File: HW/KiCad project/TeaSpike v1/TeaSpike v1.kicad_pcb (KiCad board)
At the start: 2 copper layers, 90 x 85 mm, 23 parts, among them U1 TP4056, U2 PowerBoost

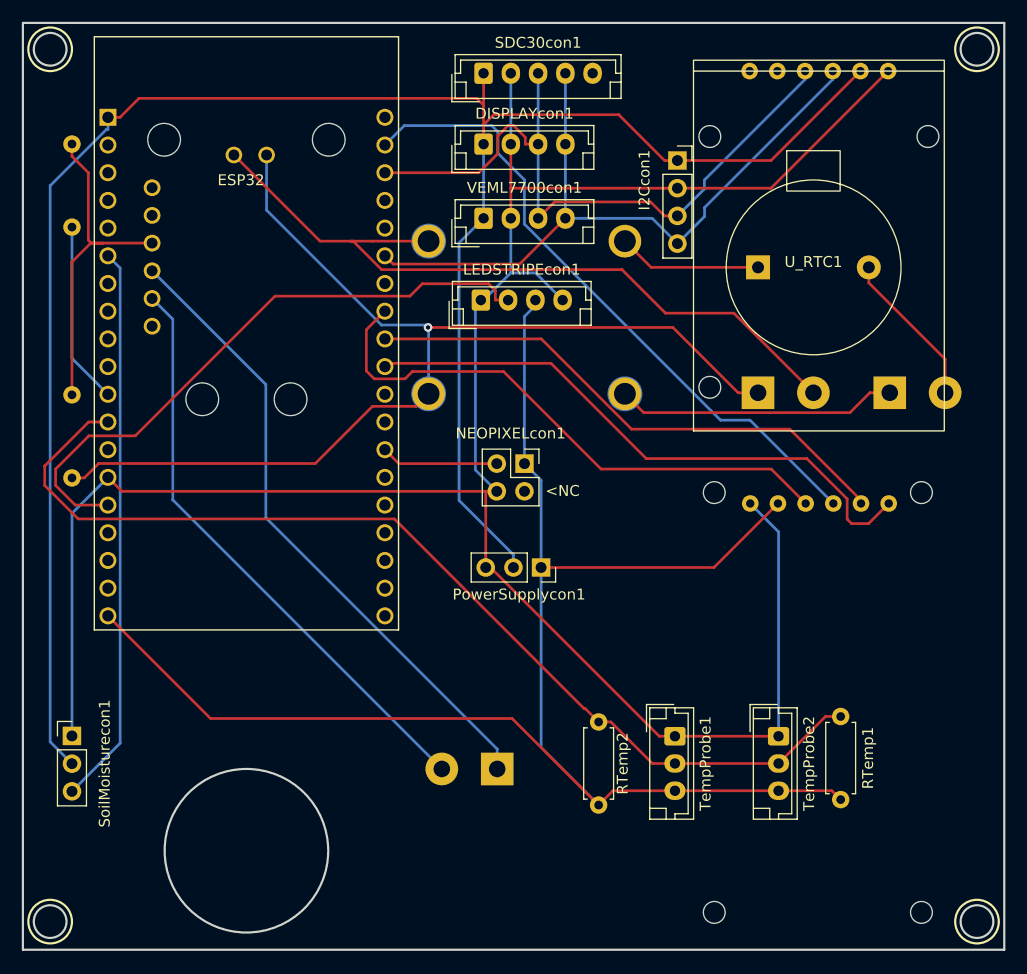
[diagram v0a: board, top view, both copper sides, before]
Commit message: Modificado circuito alimentación. Añadido aviso low bat.
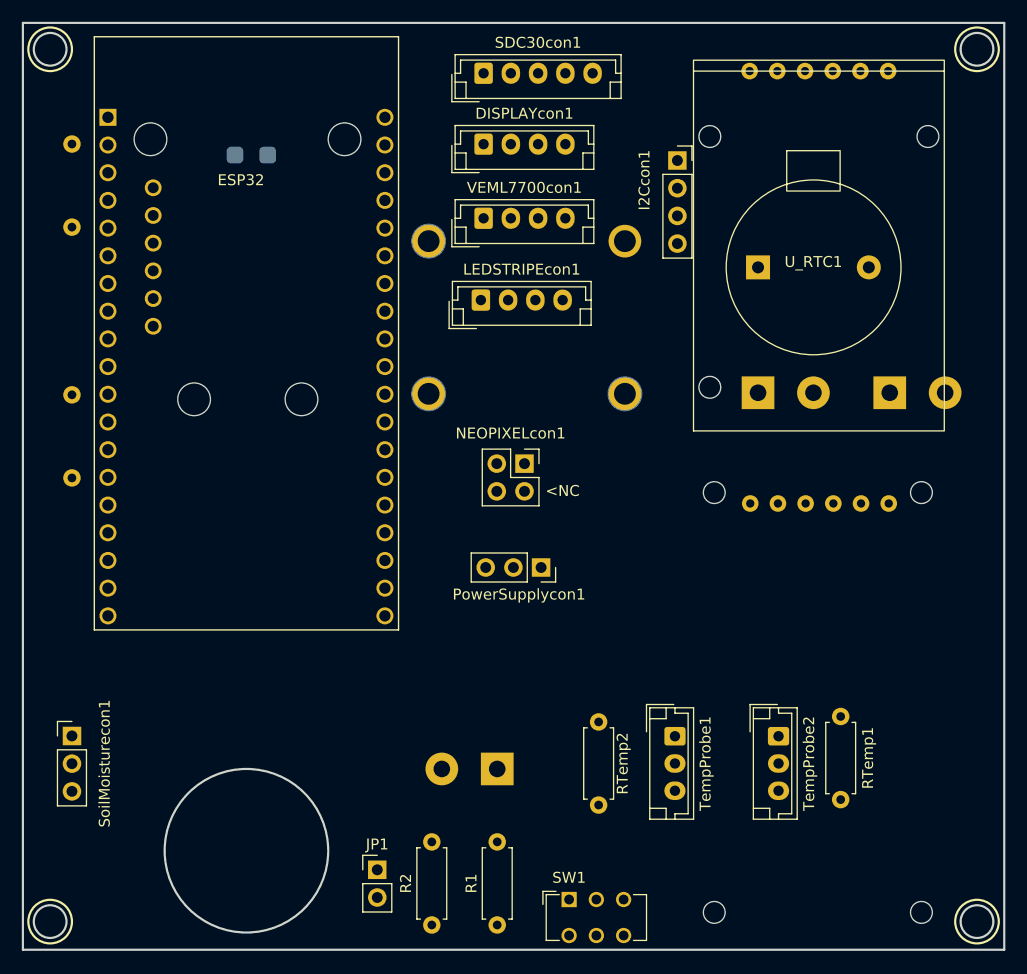
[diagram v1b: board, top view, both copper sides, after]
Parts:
- added JP1: Jumper_2_Open, Connector_PinHeader_2.54mm:PinHeader_1x02_P2.54mm_Vertical, F.Cu at (133.0, 124.8)
- added R1: 2K, Resistor_THT:R_Axial_DIN0207_L6.3mm_D2.5mm_P7.62mm_Horizontal, F.Cu at (144.0, 129.8)
- added R2: 1K, Resistor_THT:R_Axial_DIN0207_L6.3mm_D2.5mm_P7.62mm_Horizontal, F.Cu at (138.0, 129.8)
- added SW1: SW_DPDT_x2, Button_Switch_THT:SW_CuK_JS202011AQN_DPDT_Angled, F.Cu at (150.6, 127.5)
- moved U2 0.10 mm to (115.0, 44.0)
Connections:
- Batterycon1 pad 2: Net-(Batterycon1-Pad2) -> Net-(U1-Pad4)
- U1 pad 3: Net-(Batterycon1-Pad2) -> Net-(U1-Pad3)
- U1 pad 4: Net-(Batterycon1-Pad1) -> Net-(U1-Pad4)
- U2 pad 1: Net-(Batterycon1-Pad2) -> unconnected-(U2-Pad1)
- U2 pad 2: Net-(Batterycon1-Pad1) -> unconnected-(U2-Pad2)
- U2 pad 3: unconnected-(U2-Pad3) -> Net-(SW1-Pad1)
- U2 pad 4: unconnected-(U2-Pad4) -> Net-(U1-Pad4)
- U2 pad 5: Net-(R1-Pad2) -> unconnected-(U2-Pad5)
- U2 pad 6: Net-(SW_PwrB_Enable1-Pad1) -> Net-(U2-Pad6)
- U2 pad 7: Net-(SW_PwrB_Enable1-Pad2) -> Net-(U2-Pad7)
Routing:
- net GND: track 209.5 -> 0.00 mm
- net 3V3: track 186.2 -> 0.00 mm
- net 5V: track 149.0 -> 0.00 mm
- net Net-(Batterycon1-Pad1): track 99.1 -> 0.00 mm, vias 1 -> 0
- net OneWire: track 94.6 -> 0.00 mm
- net Net-(Batterycon1-Pad2): track 69.3 -> 0.00 mm
- net SDA: track 64.9 -> 0.00 mm
- net SCL: track 63.2 -> 0.00 mm
- net MOSI: track 59.8 -> 0.00 mm
- net Net-(SW_PwrB_Enable1-Pad1): track 58.8 -> 0.00 mm
- net LEDSTRIPE: track 56.7 -> 0.00 mm
- net SDcs: track 54.3 -> 0.00 mm
- net Net-(SW_PwrB_Enable1-Pad2): track 54.2 -> 0.00 mm
- net MISO: track 52.1 -> 0.00 mm
- net SoilMoisture: track 51.4 -> 0.00 mm
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
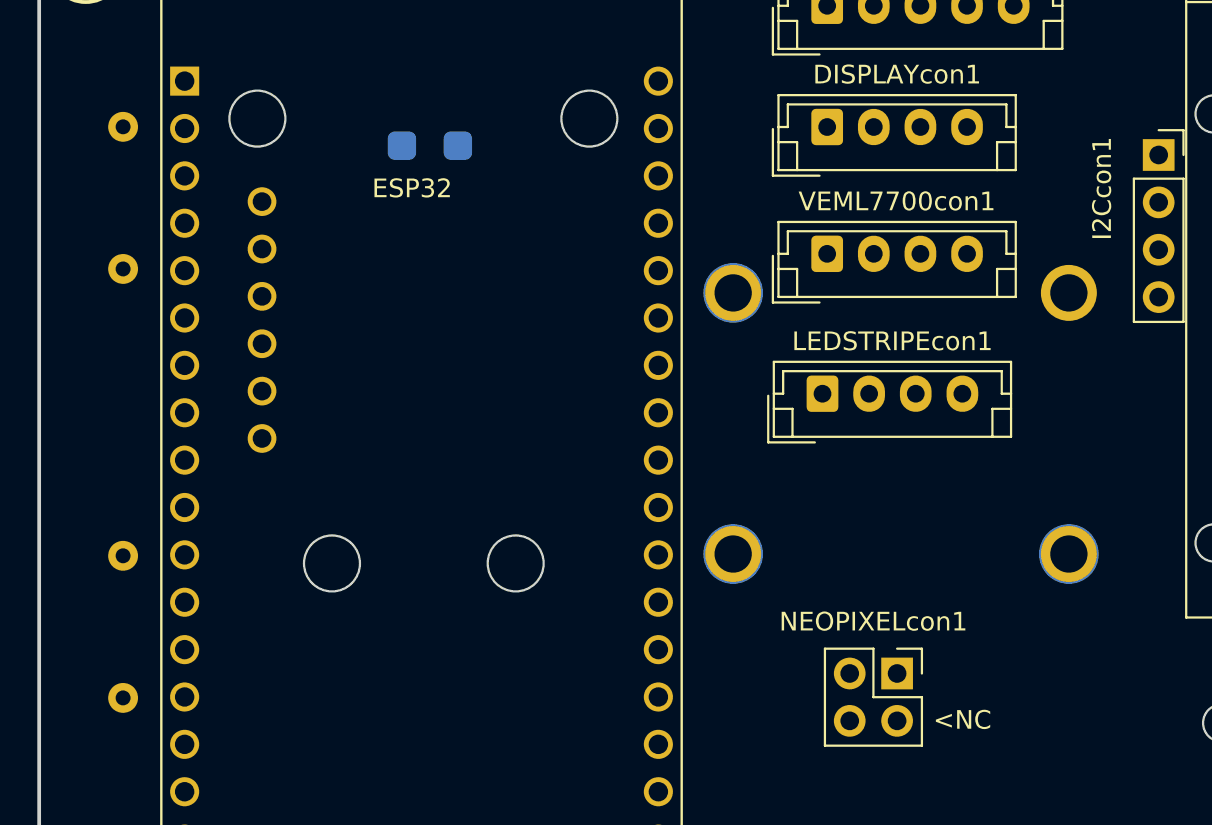
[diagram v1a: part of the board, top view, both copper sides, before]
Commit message: Versión tras revisión de Marina. Creado SpectraDSN. Falta routear las pistas
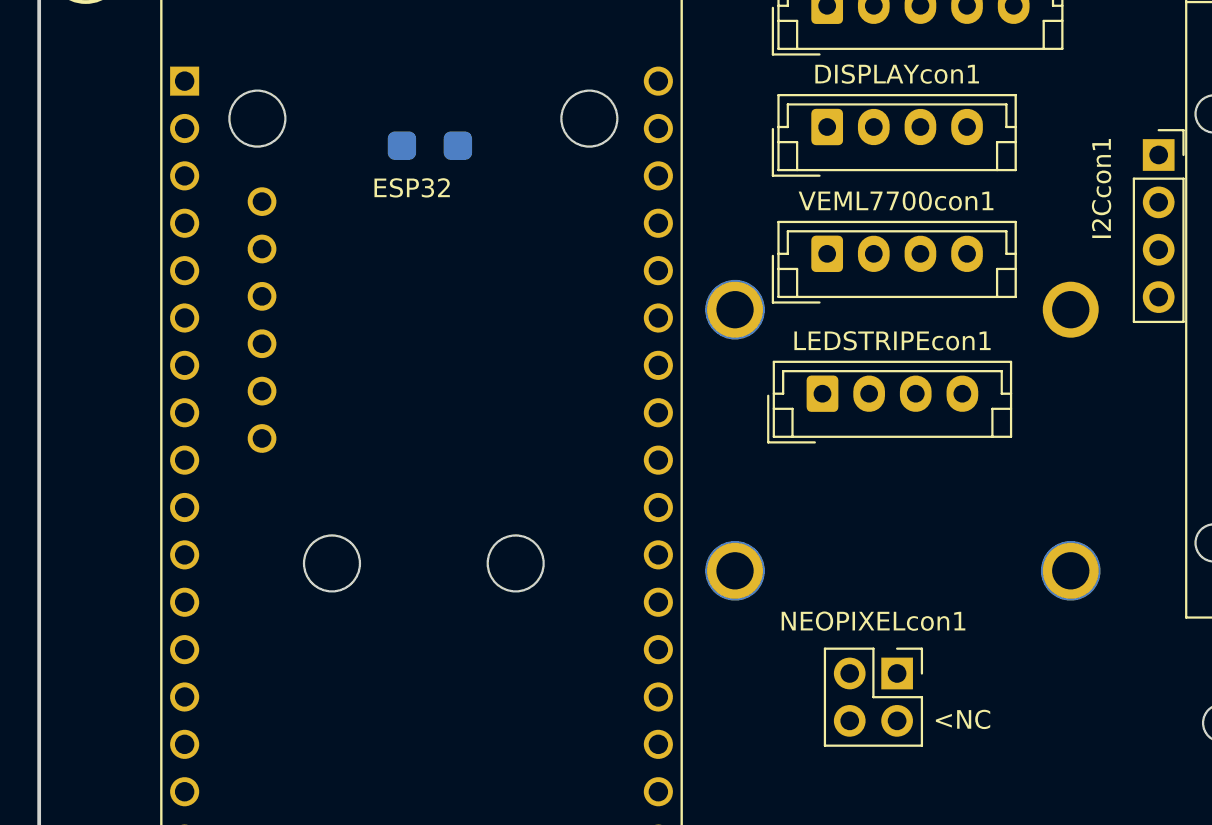
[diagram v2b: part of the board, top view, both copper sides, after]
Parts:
- removed the R1 at (105.0, 65.8)
- removed the R2 at (105.0, 81.2)
- moved U1 0.91 mm to (145.7, 60.4)

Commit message: Versión final para fabricación
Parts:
- removed SW_PwrB_Enable1: SW_DIP_x01, TerminalBlock:TerminalBlock_bornier-2_P5.08mm
- renumbered SW1 to SW_POWER
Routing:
- net GND: track 0.00 -> 231.3 mm
- net 3V3: track 0.00 -> 206.1 mm
- net 5V: track 0.00 -> 147.6 mm, vias 0 -> 1
- net Net-(Batterycon1-Pad2): track 0.00 -> 94.7 mm
- net OneWire: track 0.00 -> 82.0 mm, vias 0 -> 1
- net Net-(SW1-Pad1): track 0.00 -> 81.7 mm
- net Net-(SW1-Pad3): track 0.00 -> 76.9 mm
- net Net-(JP1-Pad1): track 0.00 -> 70.4 mm
- net SDA: track 0.00 -> 65.5 mm
- net LowBatt: track 0.00 -> 64.1 mm
- net MOSI: track 0.00 -> 63.4 mm
- net Net-(R2-Pad2): track 0.00 -> 60.4 mm
- net SCL: track 0.00 -> 59.8 mm
- net SCK: track 0.00 -> 59.0 mm
- net SDcs: track 0.00 -> 54.3 mm
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
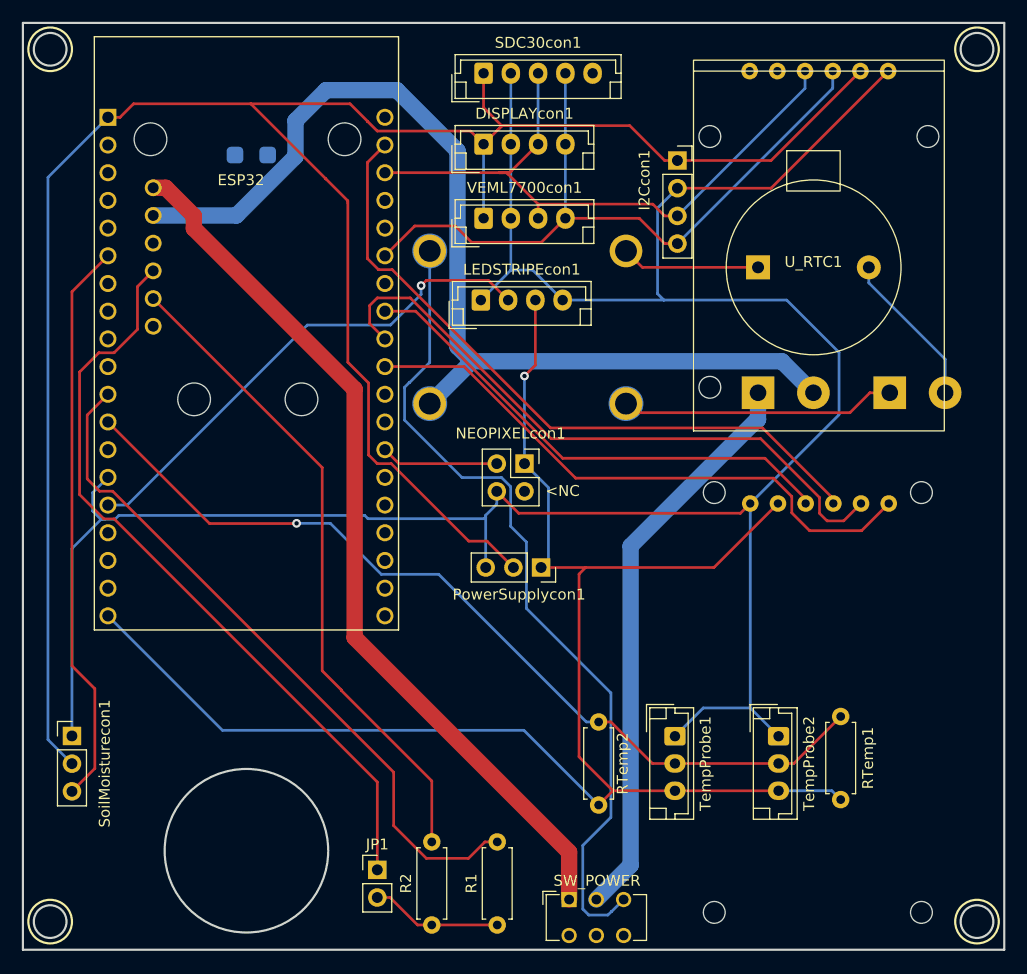
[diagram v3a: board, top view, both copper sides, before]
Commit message: Corregido ancho de pista
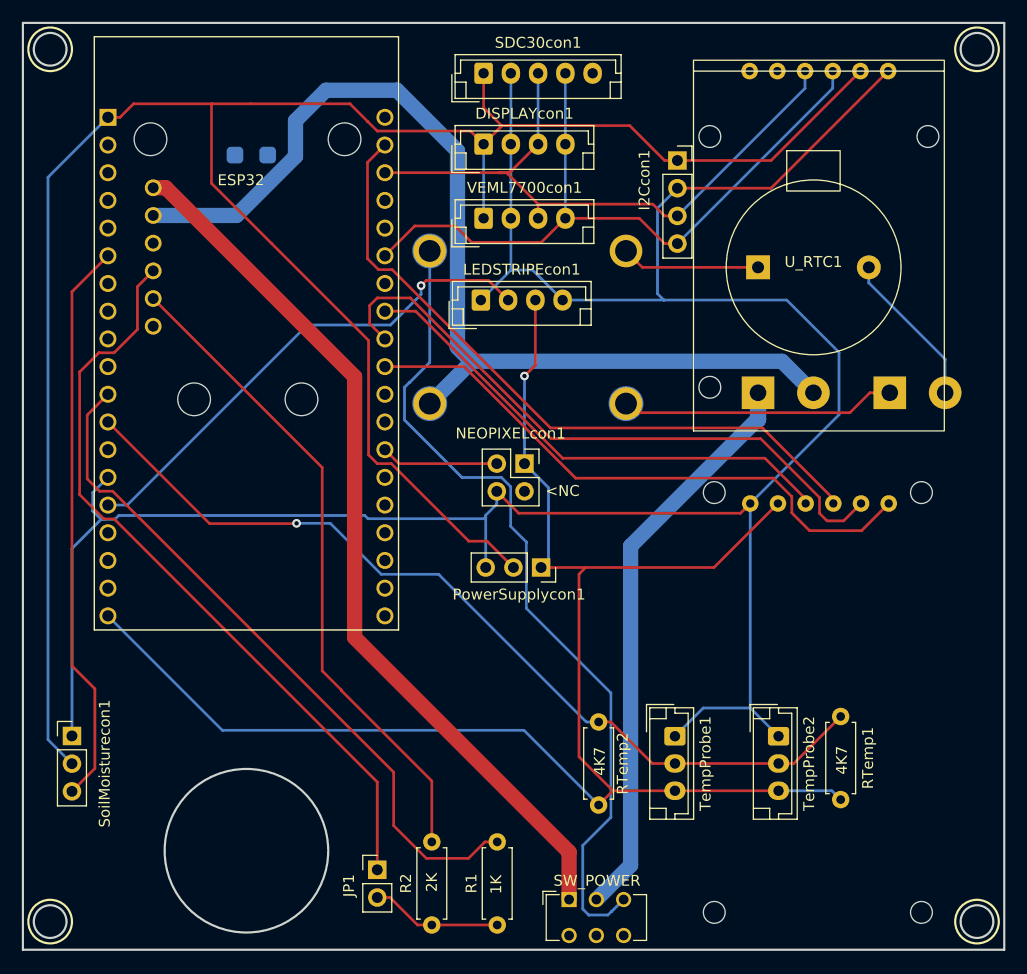
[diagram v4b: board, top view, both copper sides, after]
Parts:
- R1: value 2K -> 1K
- R2: value 1K -> 2K
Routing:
- net 3V3: track 206.1 -> 207.5 mm

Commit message: Versión fabricada
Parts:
- added G***: LOGO, LOGO, F.Cu at (173.7, 101.0)
- renumbered SDC30con1 to SCD30con1
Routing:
- net Net-(Batterycon1-Pad1): track 52.7 -> 53.3 mm
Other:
- board text added: "Spike v2.0"
- board text added: "Universidad Politécnica de Madrid"
